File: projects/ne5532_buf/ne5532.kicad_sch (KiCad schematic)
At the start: 3 parts, among them U1 NE5532

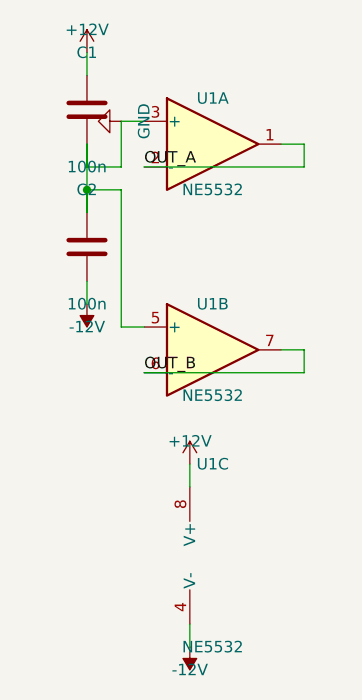
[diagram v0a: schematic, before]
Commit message: Phase 0: KiCad 10 migration + fix blind ERC parsing
- kicad-cli writes JSON reports only to -o file, never stdout; runner
  now uses a temp report file and real JSON decoding
- DetectKicadCLI exported and reused by render_sch and export_test
- KiCad 10 symbol renames (ATmega328-AU -> ATmega328-A) and pin
  numbers fixed in demos

Co-Authored-By: Claude Fable 5 <noreply@anthropic.com>
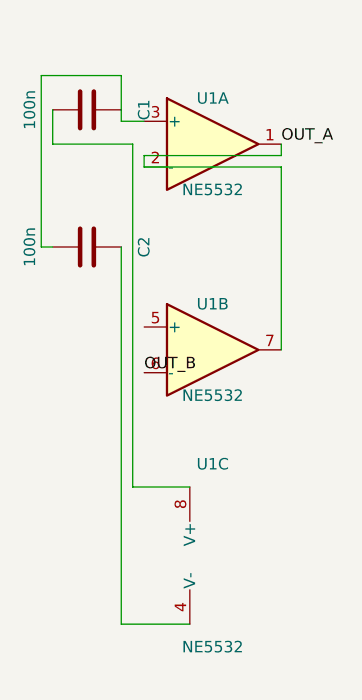
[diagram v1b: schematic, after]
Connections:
- net OUT_A: now also U1.7
- net OUT_B: no longer U1.7
- net +12V: no longer names the net of C1.1, U1.8 (V+)
- net -12V: no longer names the net of C2.2, U1.4 (V-)
- net GND: no longer names the net of C1.2, C2.1, U1.3 (+)
- net GND: no longer U1.5 (+)

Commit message: Phase 1: geometric quality gate (internal/place2/gate)
Post-hoc Enforce() guarantees zero cross-net crossings, zero wires
through symbol bodies, zero collinear overlaps: offending nets are
demoted to net labels (no geometry, identical connectivity). Wired
into connect_netlist and relayout. Same-net duplicate segments are
merged by Clean, not demoted.

Co-Authored-By: Claude Fable 5 <noreply@anthropic.com>
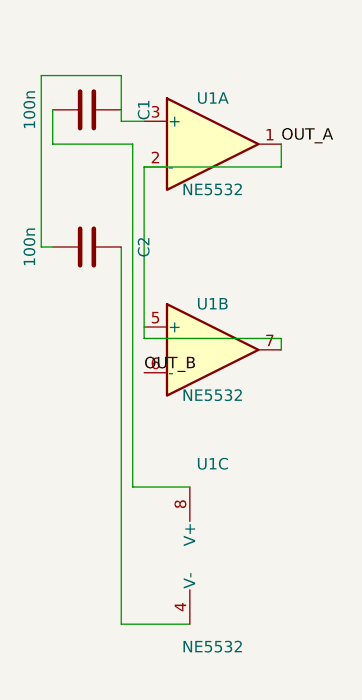
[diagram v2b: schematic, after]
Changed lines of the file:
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@@
     (instances
       (project ""
-        (path "/9b9658ab-9836-4fee-bcfc-32220a0ec7a4" (reference "U1") (unit 1)))))
+        (path "/2ca35efc-fa9e-4da3-949f-2977c9c1aafd" (reference "U1") (unit 1)))))
   (symbol (lib_id "Amplifier_Operational:NE5532")
     (at 50.8 73.66 0) (unit 2) (exclude_from_sim no) (in_bom yes) (on_board yes) (dnp no)
@@
     (instances
       (project ""
-        (path "/9b9658ab-9836-4fee-bcfc-32220a0ec7a4" (reference "U1") (unit 2)))))
+        (path "/2ca35efc-fa9e-4da3-949f-2977c9c1aafd" (reference "U1") (unit 2)))))
   (symbol (lib_id "Amplifier_Operational:NE5532")
     (at 50.8 96.52 0) (unit 3) (exclude_from_sim no) (in_bom yes) (on_board yes) (dnp no)
@@
     (instances
       (project ""
-        (path "/9b9658ab-9836-4fee-bcfc-32220a0ec7a4" (reference "U1") (unit 3)))))
+        (path "/2ca35efc-fa9e-4da3-949f-2977c9c1aafd" (reference "U1") (unit 3)))))
   (symbol (lib_id "Device:C")
     (at 36.83 46.99 90) (unit 1) (exclude_from_sim no) (in_bom yes) (on_board yes) (dnp no)
@@
     (instances
       (project ""
-        (path "/9b9658ab-9836-4fee-bcfc-32220a0ec7a4" (reference "C1") (unit 1)))))
+        (path "/2ca35efc-fa9e-4da3-949f-2977c9c1aafd" (reference "C1") (unit 1)))))
   (symbol (lib_id "Device:C")
     (at 36.83 62.23 90) (unit 1) (exclude_from_sim no) (in_bom yes) (on_board yes) (dnp no)
@@
     (instances
       (project ""
-        (path "/9b9658ab-9836-4fee-bcfc-32220a0ec7a4" (reference "C2") (unit 1)))))
+        (path "/2ca35efc-fa9e-4da3-949f-2977c9c1aafd" (reference "C2") (unit 1)))))
+  (label "OUT_A"
+    (at 58.42 50.8 0) (fields_autoplaced yes)
+    (effects
+      (font (size 1.27 1.27)) (justify left bottom))
+    (property "Intersheet References" ""
+      (at 0 0 0)
+      (effects
+        (font (size 1.27 1.27)) (hide yes))))
   (label "OUT_B"
     (at 43.18 76.2 180) (fields_autoplaced yes)
@@
       (effects
         (font (size 1.27 1.27)) (hide yes))))
-  (label "OUT_A"
-    (at 58.42 50.8 0) (fields_autoplaced yes)
-    (effects
-      (font (size 1.27 1.27)) (justify left bottom))
-    (property "Intersheet References" ""
-      (at 0 0 0)
-      (effects
-        (font (size 1.27 1.27)) (hide yes))))
-  (wire
-    (pts (xy 43.18 53.34) (xy 58.42 53.34))
-    (stroke (width 0) (type default)))
-  (wire
-    (pts (xy 58.42 53.34) (xy 58.42 73.66))
-    (stroke (width 0) (type default)))
   (wire
     (pts (xy 48.26 104.14) (xy 40.64 104.14))
@@
     (stroke (width 0) (type default)))
   (wire
-    (pts (xy 58.42 50.8) (xy 58.42 52.07))
+    (pts (xy 58.42 50.8) (xy 58.42 53.34))
     (stroke (width 0) (type default)))
   (wire
-    (pts (xy 58.42 52.07) (xy 43.18 52.07))
-    (stroke (width 0) (type default)))
-  (wire
-    (pts (xy 43.18 52.07) (xy 43.18 53.34))
+    (pts (xy 58.42 53.34) (xy 43.18 53.34))
     (stroke (width 0) (type default)))
   (wire
@@
   (wire
     (pts (xy 31.75 62.23) (xy 33.02 62.23))
+    (stroke (width 0) (type default)))
+  (wire
+    (pts (xy 43.18 53.34) (xy 43.18 72.39))
+    (stroke (width 0) (type default)))
+  (wire
+    (pts (xy 43.18 72.39) (xy 58.42 72.39))
+    (stroke (width 0) (type default)))
+  (wire
+    (pts (xy 58.42 72.39) (xy 58.42 73.66))
     (stroke (width 0) (type default))))

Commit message: Phase 2: baked template geometry + LM358 embed fix
Templates now carry hand-authored wires/junctions/labels in relative
coords; Stamp() emits them verbatim. All 5 templates rewritten with
human conventions and self-verifying tests (gate.Check==0, TraceNets
contract, exact pin-endpoint match). flattenRawSymbol now inherits
parent properties so embedded derived symbols match KiCad 10
regeneration (fixes lib_symbol_mismatch for LM358/NE5532).

Co-Authored-By: Claude Fable 5 <noreply@anthropic.com>
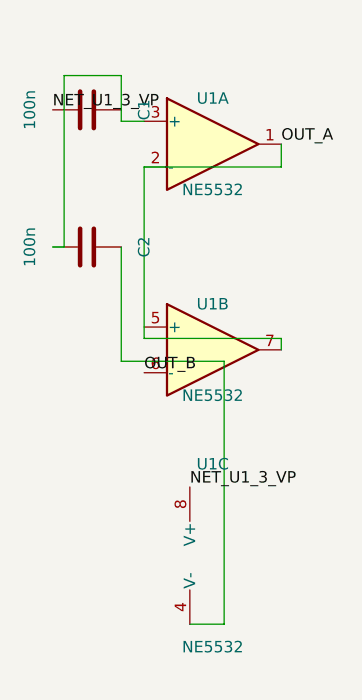
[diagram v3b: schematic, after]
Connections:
- net NET_U1_3_VP: now reaches C1.1, U1.8 (V+)
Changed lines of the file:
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@@
     (instances
       (project ""
-        (path "/2ca35efc-fa9e-4da3-949f-2977c9c1aafd" (reference "U1") (unit 1)))))
+        (path "/3b7921a3-8e25-479a-9e60-38102002f296" (reference "U1") (unit 1)))))
   (symbol (lib_id "Amplifier_Operational:NE5532")
     (at 50.8 73.66 0) (unit 2) (exclude_from_sim no) (in_bom yes) (on_board yes) (dnp no)
@@
     (instances
       (project ""
-        (path "/2ca35efc-fa9e-4da3-949f-2977c9c1aafd" (reference "U1") (unit 2)))))
+        (path "/3b7921a3-8e25-479a-9e60-38102002f296" (reference "U1") (unit 2)))))
   (symbol (lib_id "Amplifier_Operational:NE5532")
     (at 50.8 96.52 0) (unit 3) (exclude_from_sim no) (in_bom yes) (on_board yes) (dnp no)
@@
     (instances
       (project ""
-        (path "/2ca35efc-fa9e-4da3-949f-2977c9c1aafd" (reference "U1") (unit 3)))))
+        (path "/3b7921a3-8e25-479a-9e60-38102002f296" (reference "U1") (unit 3)))))
   (symbol (lib_id "Device:C")
     (at 36.83 46.99 90) (unit 1) (exclude_from_sim no) (in_bom yes) (on_board yes) (dnp no)
@@
     (instances
       (project ""
-        (path "/2ca35efc-fa9e-4da3-949f-2977c9c1aafd" (reference "C1") (unit 1)))))
+        (path "/3b7921a3-8e25-479a-9e60-38102002f296" (reference "C1") (unit 1)))))
   (symbol (lib_id "Device:C")
     (at 36.83 62.23 90) (unit 1) (exclude_from_sim no) (in_bom yes) (on_board yes) (dnp no)
@@
     (instances
       (project ""
-        (path "/2ca35efc-fa9e-4da3-949f-2977c9c1aafd" (reference "C2") (unit 1)))))
+        (path "/3b7921a3-8e25-479a-9e60-38102002f296" (reference "C2") (unit 1)))))
   (label "OUT_A"
     (at 58.42 50.8 0) (fields_autoplaced yes)
@@
         (font (size 1.27 1.27)) (hide yes))))
   (wire
-    (pts (xy 48.26 104.14) (xy 40.64 104.14))
-    (stroke (width 0) (type default)))
-  (wire
-    (pts (xy 40.64 104.14) (xy 40.64 62.23))
-    (stroke (width 0) (type default)))
-  (wire
-    (pts (xy 48.26 88.9) (xy 41.91 88.9))
-    (stroke (width 0) (type default)))
-  (wire
-    (pts (xy 41.91 88.9) (xy 41.91 50.8))
-    (stroke (width 0) (type default)))
-  (wire
-    (pts (xy 41.91 50.8) (xy 33.02 50.8))
-    (stroke (width 0) (type default)))
-  (wire
-    (pts (xy 33.02 50.8) (xy 33.02 46.99))
-    (stroke (width 0) (type default)))
-  (wire
     (pts (xy 58.42 50.8) (xy 58.42 53.34))
     (stroke (width 0) (type default)))
@@
     (stroke (width 0) (type default)))
   (wire
-    (pts (xy 40.64 43.18) (xy 31.75 43.18))
+    (pts (xy 40.64 43.18) (xy 34.29 43.18))
     (stroke (width 0) (type default)))
   (wire
-    (pts (xy 31.75 43.18) (xy 31.75 62.23))
+    (pts (xy 34.29 43.18) (xy 34.29 62.23))
     (stroke (width 0) (type default)))
   (wire
-    (pts (xy 31.75 62.23) (xy 33.02 62.23))
+    (pts (xy 34.29 62.23) (xy 33.02 62.23))
     (stroke (width 0) (type default)))
   (wire
@@
   (wire
     (pts (xy 58.42 72.39) (xy 58.42 73.66))
-    (stroke (width 0) (type default))))
+    (stroke (width 0) (type default)))
+  (wire
+    (pts (xy 48.26 104.14) (xy 52.07 104.14))
+    (stroke (width 0) (type default)))
+  (wire
+    (pts (xy 52.07 104.14) (xy 52.07 74.93))
+    (stroke (width 0) (type default)))
+  (wire
+    (pts (xy 52.07 74.93) (xy 40.64 74.93))
+    (stroke (width 0) (type default)))
+  (wire
+    (pts (xy 40.64 74.93) (xy 40.64 62.23))
+    (stroke (width 0) (type default)))
+  (label "NET_U1_3_VP"
+    (at 48.26 88.9 0) (fields_autoplaced yes)
+    (effects
+      (font (size 1.27 1.27)) (justify left bottom))
+    (property "Intersheet References" ""
+      (at 0 0 0)
+      (effects
+        (font (size 1.27 1.27)) (hide yes))))
+  (label "NET_U1_3_VP"
+    (at 33.02 46.99 0) (fields_autoplaced yes)
+    (effects
+      (font (size 1.27 1.27)) (justify left bottom))
+    (property "Intersheet References" ""
+      (at 0 0 0)
+      (effects
+        (font (size 1.27 1.27)) (hide yes)))))

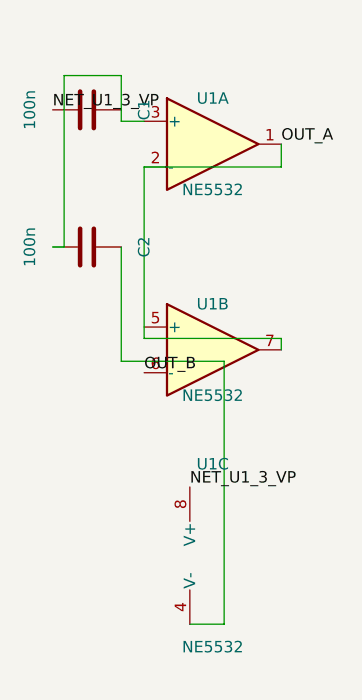
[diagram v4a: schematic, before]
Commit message: Phase 4: per-pin power rail policy + full pipeline determinism
Power nets are never routed: every pin on a rail gets its own power
symbol (GND down, VCC up) with a 2.54mm stub; PWR_FLAG emitted after
the gate for undriven power_in nets. Determinism: cluster detection
and TraceNets no longer depend on Go map iteration order (refOrder
slices, sorted canonical net naming). 6/6 identical runs on vreg and
mcu demos; vreg ERC now has zero errors.

Co-Authored-By: Claude Fable 5 <noreply@anthropic.com>
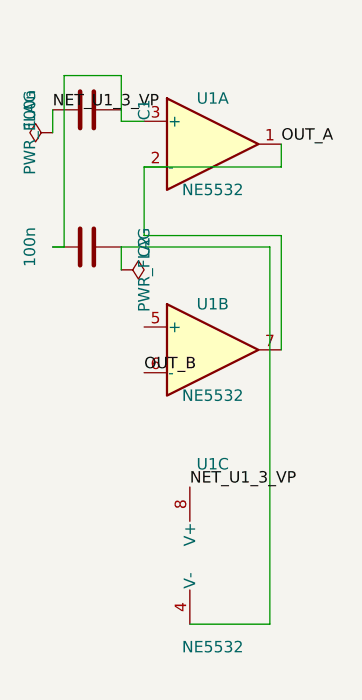
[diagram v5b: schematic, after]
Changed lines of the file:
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@@
     (instances
       (project ""
-        (path "/81f78e22-837c-4c35-9895-4c65a4dff690" (reference "U1") (unit 1)))))
+        (path "/c6e72297-c922-456a-906c-551ff21bd294" (reference "U1") (unit 1)))))
   (symbol (lib_id "Amplifier_Operational:NE5532")
     (at 50.8 73.66 0) (unit 2) (exclude_from_sim no) (in_bom yes) (on_board yes) (dnp no)
@@
     (instances
       (project ""
-        (path "/81f78e22-837c-4c35-9895-4c65a4dff690" (reference "U1") (unit 2)))))
+        (path "/c6e72297-c922-456a-906c-551ff21bd294" (reference "U1") (unit 2)))))
   (symbol (lib_id "Amplifier_Operational:NE5532")
     (at 50.8 96.52 0) (unit 3) (exclude_from_sim no) (in_bom yes) (on_board yes) (dnp no)
@@
     (instances
       (project ""
-        (path "/81f78e22-837c-4c35-9895-4c65a4dff690" (reference "U1") (unit 3)))))
+        (path "/c6e72297-c922-456a-906c-551ff21bd294" (reference "U1") (unit 3)))))
   (symbol (lib_id "Device:C")
     (at 36.83 46.99 90) (unit 1) (exclude_from_sim no) (in_bom yes) (on_board yes) (dnp no)
@@
     (instances
       (project ""
-        (path "/81f78e22-837c-4c35-9895-4c65a4dff690" (reference "C1") (unit 1)))))
+        (path "/c6e72297-c922-456a-906c-551ff21bd294" (reference "C1") (unit 1)))))
   (symbol (lib_id "Device:C")
     (at 36.83 62.23 90) (unit 1) (exclude_from_sim no) (in_bom yes) (on_board yes) (dnp no)
@@
     (instances
       (project ""
-        (path "/81f78e22-837c-4c35-9895-4c65a4dff690" (reference "C2") (unit 1)))))
+        (path "/c6e72297-c922-456a-906c-551ff21bd294" (reference "C2") (unit 1)))))
   (label "OUT_A"
     (at 58.42 50.8 0) (fields_autoplaced yes)
@@
         (font (size 1.27 1.27)) (hide yes))))
   (wire
+    (pts (xy 48.26 104.14) (xy 57.15 104.14))
+    (stroke (width 0) (type default)))
+  (wire
+    (pts (xy 57.15 104.14) (xy 57.15 62.23))
+    (stroke (width 0) (type default)))
+  (wire
+    (pts (xy 57.15 62.23) (xy 40.64 62.23))
+    (stroke (width 0) (type default)))
+  (wire
+    (pts (xy 43.18 48.26) (xy 40.64 48.26))
+    (stroke (width 0) (type default)))
+  (wire
+    (pts (xy 40.64 48.26) (xy 40.64 46.99))
+    (stroke (width 0) (type default)))
+  (wire
+    (pts (xy 40.64 46.99) (xy 40.64 43.18))
+    (stroke (width 0) (type default)))
+  (wire
+    (pts (xy 40.64 43.18) (xy 34.29 43.18))
+    (stroke (width 0) (type default)))
+  (wire
+    (pts (xy 34.29 43.18) (xy 34.29 62.23))
+    (stroke (width 0) (type default)))
+  (wire
+    (pts (xy 34.29 62.23) (xy 33.02 62.23))
+    (stroke (width 0) (type default)))
+  (wire
     (pts (xy 58.42 50.8) (xy 58.42 53.34))
     (stroke (width 0) (type default)))
@@
     (stroke (width 0) (type default)))
   (wire
-    (pts (xy 43.18 48.26) (xy 40.64 48.26))
-    (stroke (width 0) (type default)))
-  (wire
-    (pts (xy 40.64 48.26) (xy 40.64 46.99))
-    (stroke (width 0) (type default)))
-  (wire
-    (pts (xy 40.64 46.99) (xy 40.64 43.18))
-    (stroke (width 0) (type default)))
-  (wire
-    (pts (xy 40.64 43.18) (xy 34.29 43.18))
-    (stroke (width 0) (type default)))
-  (wire
-    (pts (xy 34.29 43.18) (xy 34.29 62.23))
-    (stroke (width 0) (type default)))
-  (wire
-    (pts (xy 34.29 62.23) (xy 33.02 62.23))
-    (stroke (width 0) (type default)))
-  (wire
-    (pts (xy 43.18 53.34) (xy 43.18 72.39))
-    (stroke (width 0) (type default)))
-  (wire
-    (pts (xy 43.18 72.39) (xy 58.42 72.39))
-    (stroke (width 0) (type default)))
-  (wire
-    (pts (xy 58.42 72.39) (xy 58.42 73.66))
-    (stroke (width 0) (type default)))
-  (wire
-    (pts (xy 48.26 104.14) (xy 52.07 104.14))
-    (stroke (width 0) (type default)))
-  (wire
-    (pts (xy 52.07 104.14) (xy 52.07 74.93))
-    (stroke (width 0) (type default)))
-  (wire
-    (pts (xy 52.07 74.93) (xy 40.64 74.93))
-    (stroke (width 0) (type default)))
-  (wire
-    (pts (xy 40.64 74.93) (xy 40.64 62.23))
+    (pts (xy 43.18 53.34) (xy 43.18 60.96))
+    (stroke (width 0) (type default)))
+  (wire
+    (pts (xy 43.18 60.96) (xy 58.42 60.96))
+    (stroke (width 0) (type default)))
+  (wire
+    (pts (xy 58.42 60.96) (xy 58.42 73.66))
     (stroke (width 0) (type default)))
   (label "NET_U1_3_VP"
@@
       (at 0 0 0)
       (effects
-        (font (size 1.27 1.27)) (hide yes)))))
+        (font (size 1.27 1.27)) (hide yes))))
+  (symbol (lib_id "power:PWR_FLAG")
+    (at 33.02 49.53 90) (unit 1) (exclude_from_sim no) (in_bom no) (on_board no) (dnp no)
+    (property "Reference" "#FLG01"
+      (at 33.02 49.53 0)
+      (effects
+        (font (size 1.27 1.27)) (hide yes)))
+    (property "Value" "PWR_FLAG"
+      (at 30.48 49.53 0)
+      (effects
+        (font (size 1.27 1.27))))
+    (property "Footprint" ""
+      (at 33.02 49.53 0)
+      (effects
+        (font (size 1.27 1.27)) (hide yes)))
+    (property "Datasheet" ""
+      (at 33.02 49.53 0)
+      (effects
+        (font (size 1.27 1.27)) (hide yes)))
+    (property "Description" ""
+      (at 33.02 49.53 0)
+      (effects
+        (font (size 1.27 1.27)) (hide yes)))
+    (pin "1")
+    (instances
+      (project ""
+        (path "/c6e72297-c922-456a-906c-551ff21bd294" (reference "#FLG01") (unit 1)))))
+  (wire
+    (pts (xy 33.02 46.99) (xy 33.02 49.53))
+    (stroke (width 0) (type default)))
+  (symbol (lib_id "power:PWR_FLAG")
+    (at 40.64 64.77 270) (unit 1) (exclude_from_sim no) (in_bom no) (on_board no) (dnp no)
+    (property "Reference" "#FLG02"
+      (at 40.64 64.77 0)
+      (effects
+        (font (size 1.27 1.27)) (hide yes)))
+    (property "Value" "PWR_FLAG"
+      (at 43.18 64.77 0)
+      (effects
+        (font (size 1.27 1.27))))
+    (property "Footprint" ""
+      (at 40.64 64.77 0)
+      (effects
+        (font (size 1.27 1.27)) (hide yes)))
+    (property "Datasheet" ""
+      (at 40.64 64.77 0)
+      (effects
+        (font (size 1.27 1.27)) (hide yes)))
+    (property "Description" ""
+      (at 40.64 64.77 0)
+      (effects
+        (font (size 1.27 1.27)) (hide yes)))
+    (pin "1")
+    (instances
+      (project ""
+        (path "/c6e72297-c922-456a-906c-551ff21bd294" (reference "#FLG02") (unit 1)))))
+  (wire
+    (pts (xy 40.64 62.23) (xy 40.64 64.77))
+    (stroke (width 0) (type default))))
